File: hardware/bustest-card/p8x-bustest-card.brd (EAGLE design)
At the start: 160 x 100 mm, 62 parts, among them J1 MABC96R, J2 PROBE 2x5, U1 MCP23S17, U2 MCP23S17, U3 MCP23S17, U4 MCP23S17, U5 MCP23S17, U6 74HCT244, U7 74HCT244

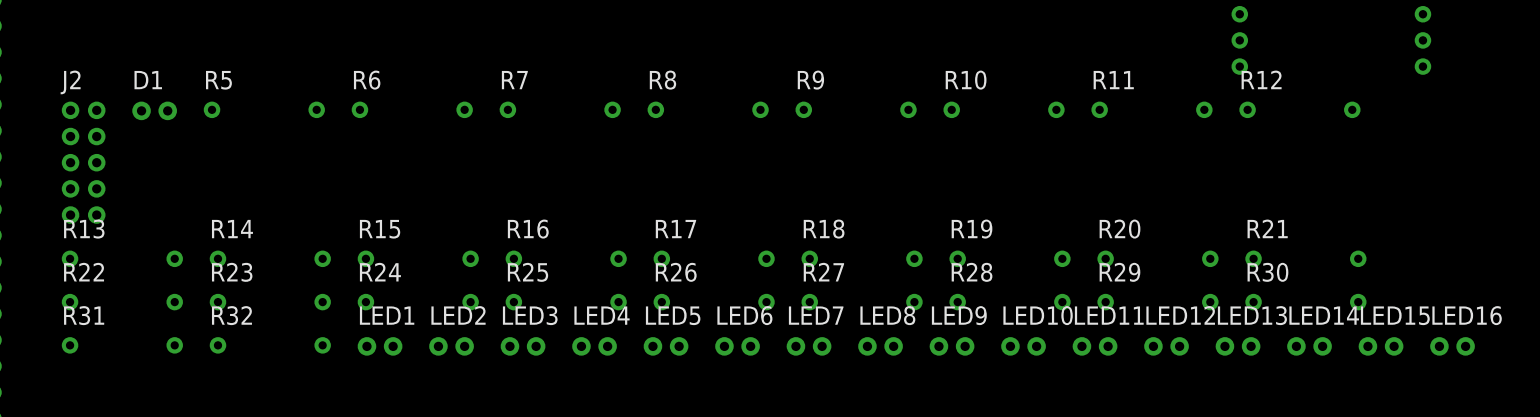
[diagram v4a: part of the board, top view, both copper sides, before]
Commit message: refactor(bustest): resistor packaging policy — DIP-16 nets, discrete for 1s/2s
Replaces the brief all-discrete resistor decision with a packaging rule:

  - DIP-16 isolated networks (new RNISO8D device) for 8-way isolated banks:
      RN1  probe-LED current limit   8x330R
      RN2  status-LED current limit  8x330R
      RN3  probe series (protection) 8x1K
  - SIP-8 / 9-pin bussed for pull-ups/downs (already true of RN1/RNP on
    backplane/cf/io; nothing on bustest needs it)
  - discrete only for 1s and 2s: bustest R5-R8 (5V-sense + MISO dividers)

Why DIP-16 and not SIP: these three banks are isolated series elements (a
different net on both ends of every leg), so a bussed SIP-8 would short all
eight legs on its shared COM. And 8 isolated resistors need 16 terminals, so
the isolated part is a 16-pin package. Chose DIP-16 over the existing SIP-16
RNISO8 per the packaging policy.

New device RNISO8D: electrically identical to RNISO8 (8 isolated resistors) but
in a 16-pin DIP with the standard isolated pinout (R_i between pin i and pin
17-i, same as DIP8SW / LEDARR8).

Part count 62 -> 41 (three networks replace 24 discretes). Verified: all RN A/B
pins wired to the correct series nets, LED anodes still on the network outputs,
caps still 7, 41 parts fit 160x100 (3 rows, x_max 158.5). RNISO8D is only used
by bustest, so all eight other boards are byte-identical. BACKLOG note updated
to the policy (supersedes the discrete-resistors note).

Co-Authored-By: Claude Opus 4.8 <noreply@anthropic.com>
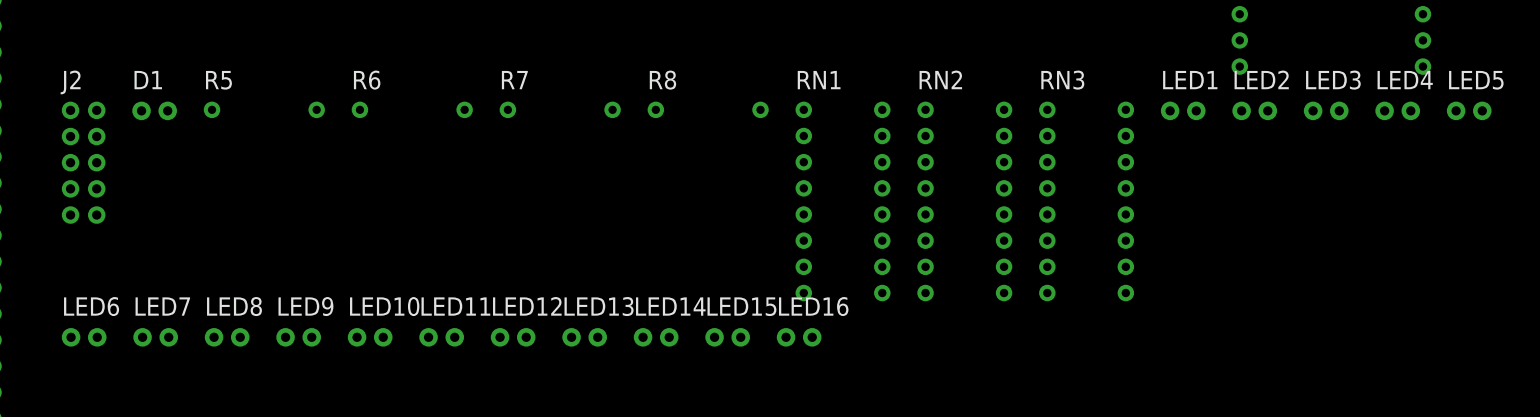
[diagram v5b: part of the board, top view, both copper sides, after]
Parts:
- removed R10, R11, R12, R13, R14, R15, R16, R17, R18, R19, R20, R21, R22, R23, R24, R9: 330R, p8x:R_AXIAL
- removed R25, R26, R27, R28, R29, R30, R31, R32: 1K, p8x:R_AXIAL
- added RN1, RN2: 8x330R, p8x:DIP16
- added RN3: 8x1K, p8x:DIP16
- moved LED1 81.2 mm to (310.1, 42.6)
- moved LED2 81.2 mm to (317.0, 42.6)
- moved LED3 81.2 mm to (323.9, 42.6)
- moved LED4 81.2 mm to (330.9, 42.6)
- moved LED5 81.2 mm to (337.8, 42.6)
- moved LED10 63.4 mm to (231.1, 20.7)
- moved LED11 63.4 mm to (238.1, 20.7)
- moved LED12 63.4 mm to (245.0, 20.7)
- moved LED13 63.4 mm to (251.9, 20.7)
- moved LED14 63.4 mm to (258.9, 20.7)
- moved LED15 63.4 mm to (265.8, 20.7)
- moved LED16 63.4 mm to (272.8, 20.7)
- moved LED6 63.4 mm to (203.4, 20.7)
- moved LED7 63.4 mm to (210.3, 20.7)
- moved LED8 63.4 mm to (217.2, 20.7)
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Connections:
- net LK_PR0: now also RN1.16; no longer R9.2
- net LK_PR1: now also RN1.15; no longer R10.2
- net LK_PR2: now also RN1.14; no longer R11.2
- net LK_PR3: now also RN1.13; no longer R12.2
- net LK_PR4: now also RN1.12; no longer R13.2
- net LK_PR5: now also RN1.11; no longer R14.2
- net LK_PR6: now also RN1.10; no longer R15.2
- net LK_PR7: now also RN1.9; no longer R16.2
- net L_PR0: now also RN1.1; no longer R9.1
- net L_PR1: now also RN1.2; no longer R10.1
- net L_PR2: now also RN1.3; no longer R11.1
- net L_PR3: now also RN1.4; no longer R12.1
- net L_PR4: now also RN1.5; no longer R13.1
- net L_PR5: now also RN1.6; no longer R14.1
- net L_PR6: now also RN1.7; no longer R15.1
- net L_PR7: now also RN1.8; no longer R16.1
- net PR0: now also RN3.1; no longer R25.1
- net PR1: now also RN3.2; no longer R26.1
- net PR2: now also RN3.3; no longer R27.1
- net PR3: now also RN3.4; no longer R28.1
- net PR4: now also RN3.5; no longer R29.1
- net PR5: now also RN3.6; no longer R30.1
- net PR6: now also RN3.7; no longer R31.1
- net PR7: now also RN3.8; no longer R32.1
- net PRJ0: now also RN3.16; no longer R25.2
- net PRJ1: now also RN3.15; no longer R26.2
- net PRJ2: now also RN3.14; no longer R27.2
- net PRJ3: now also RN3.13; no longer R28.2
- net PRJ4: now also RN3.12; no longer R29.2
- net PRJ5: now also RN3.11; no longer R30.2
- net PRJ6: now also RN3.10; no longer R31.2
- net PRJ7: now also RN3.9; no longer R32.2
- net ST0: now also RN2.1; no longer R17.1
- net ST1: now also RN2.2; no longer R18.1
- net ST2: now also RN2.3; no longer R19.1
- net ST3: now also RN2.4; no longer R20.1
- net ST4: now also RN2.5; no longer R21.1
- net ST5: now also RN2.6; no longer R22.1
- net ST6: now also RN2.7; no longer R23.1
- net ST7: now also RN2.8; no longer R24.1
- net STK0: now also RN2.16; no longer R17.2
- net STK1: now also RN2.15; no longer R18.2
- net STK2: now also RN2.14; no longer R19.2
- net STK3: now also RN2.13; no longer R20.2
- net STK4: now also RN2.12; no longer R21.2
- net STK5: now also RN2.11; no longer R22.2
- net STK6: now also RN2.10; no longer R23.2
- net STK7: now also RN2.9; no longer R24.2
